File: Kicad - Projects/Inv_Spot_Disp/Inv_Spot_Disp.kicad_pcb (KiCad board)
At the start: 2 copper layers, 137.8 x 68.7 mm, 42 parts, among them J1 PWM_Out, J2 Power_Supply, J3 Current_Sense, J4 Prog, SW1 1, SW2 2, SW3 3, SW4 4, SW5 SW_Push, U1 STM32F030F4Px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

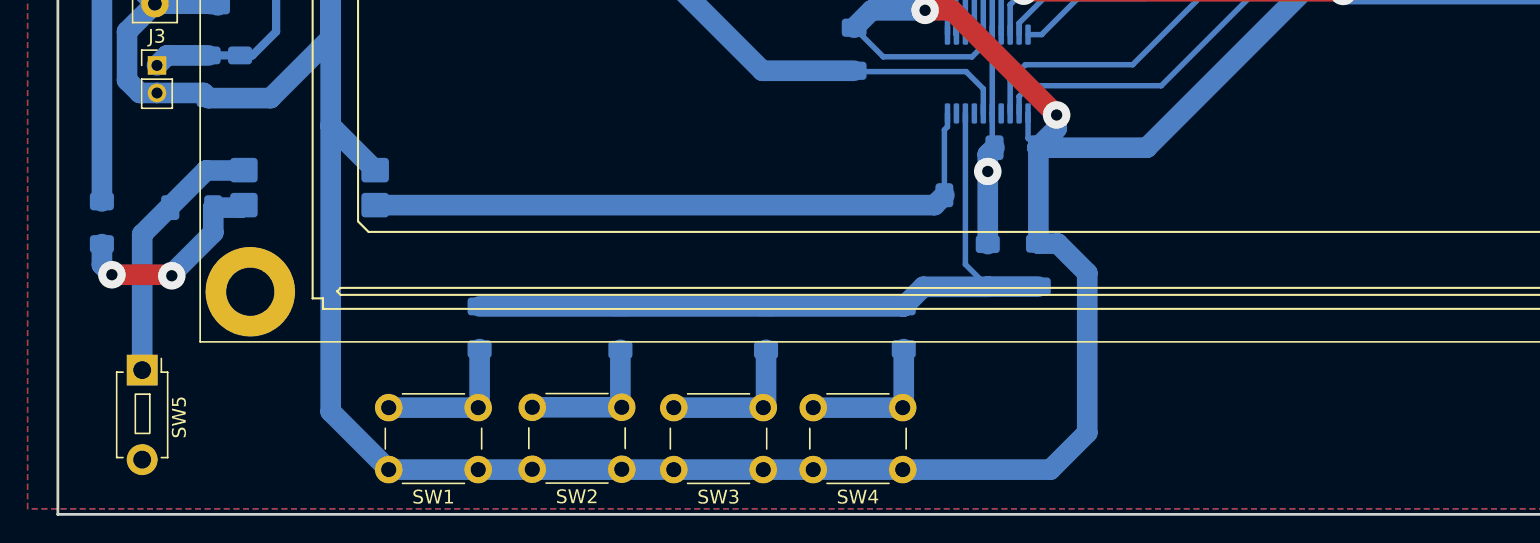
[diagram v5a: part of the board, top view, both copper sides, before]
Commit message: Ajustes de Isolamento e Espaçamento
Ajustes no isolamento de trilhas de alta tensão na placa de potência e no espaçamento dos capacitores dos IGBTs

Ajustes nas posições de componentes na placa de display

Ajustado ADC para aumentar período de amostragem
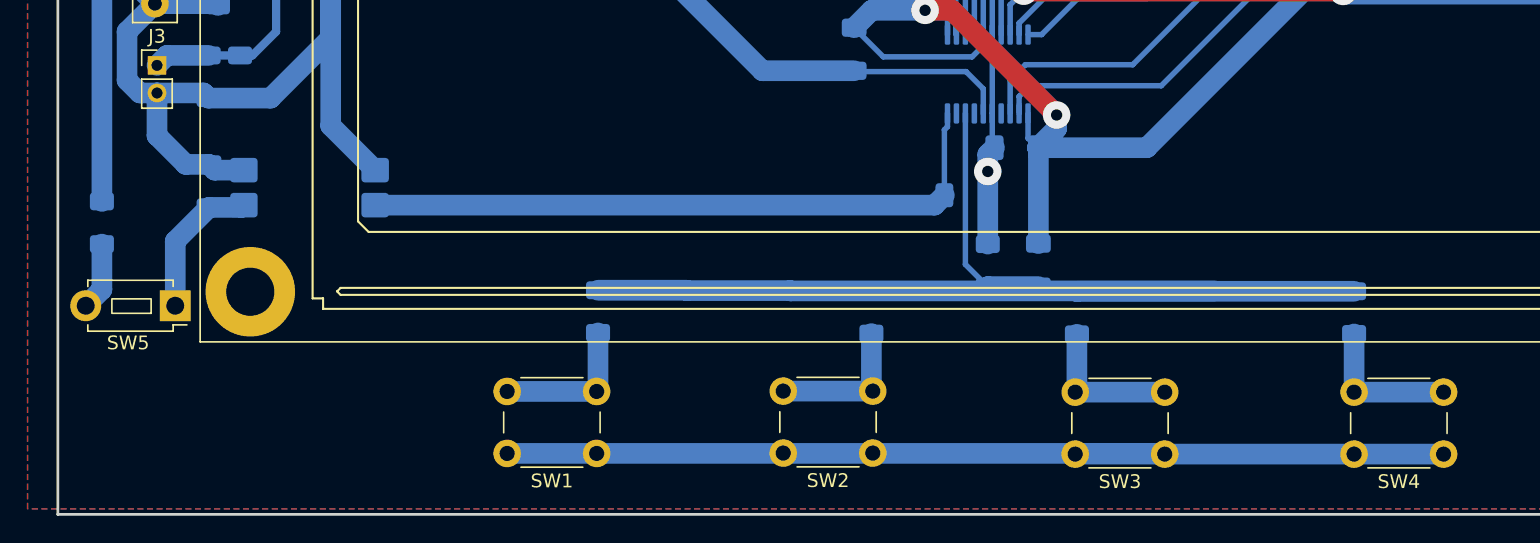
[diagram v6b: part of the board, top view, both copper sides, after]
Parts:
- moved SW4 39.3 mm to (129.1, 113.7)
- moved R5 32.7 mm to (122.6, 103.4)
- moved SW3 29.2 mm to (108.9, 113.7)
- moved R4 22.6 mm to (102.5, 103.4)
- moved R3 18.3 mm to (87.6, 103.4)
- moved SW2 18.3 mm to (87.7, 113.6)
- moved SW1 8.68 mm to (67.6, 113.6)
- moved R2 8.68 mm to (67.7, 103.3)
- moved SW5 5.26 mm to (37.0, 102.9), turned to 180 degrees
- moved C9 2.01 mm to (39.5, 94.2), turned to 90 degrees
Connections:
- C9 pad 2: Net-(C9-Pad2) -> GND
- R8 pad 1: Net-(C9-Pad1) -> Net-(R8-Pad1)
- SW5 pad 1: Net-(C9-Pad2) -> Net-(C9-Pad1)
- SW5 pad 2: Earth -> Net-(R8-Pad1)
- U6 pad 2: Net-(C9-Pad2) -> GND
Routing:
- net Display_ADC: track 54.4 -> 81.9 mm
- net Net-(C9-Pad2): track 19.2 -> 0.00 mm
- net GND: track 404.7 -> 394.4 mm
- net Net-(R8-Pad1): track 0.00 -> 4.96 mm
- net Net-(C9-Pad1): track 15.4 -> 10.8 mm, vias 2 -> 0

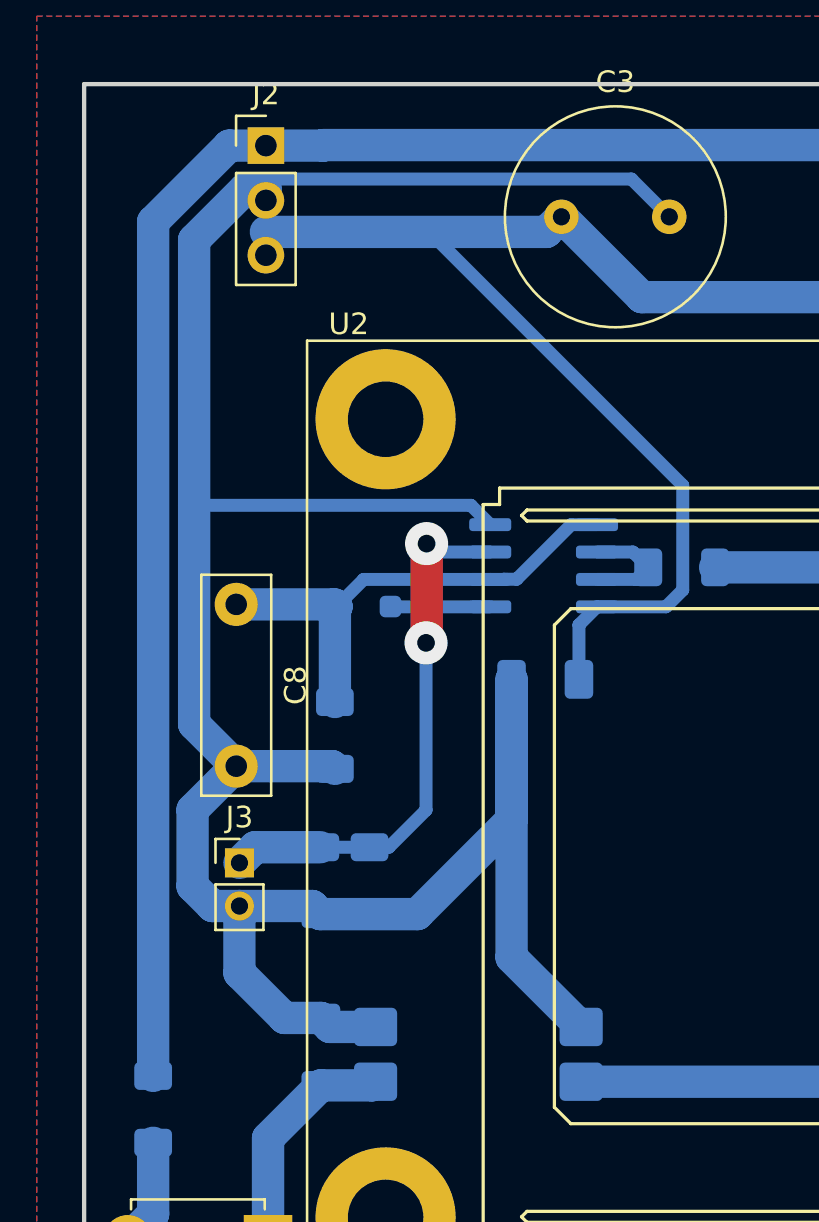
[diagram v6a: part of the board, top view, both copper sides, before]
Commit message: Ajustes de Esquemático / Layout
Ajustado símbolo da chave bimetálica na linha de 15V para proteção térmica

Ajustada trilhas de PWM que estavam sendo cobertas por um capacitor
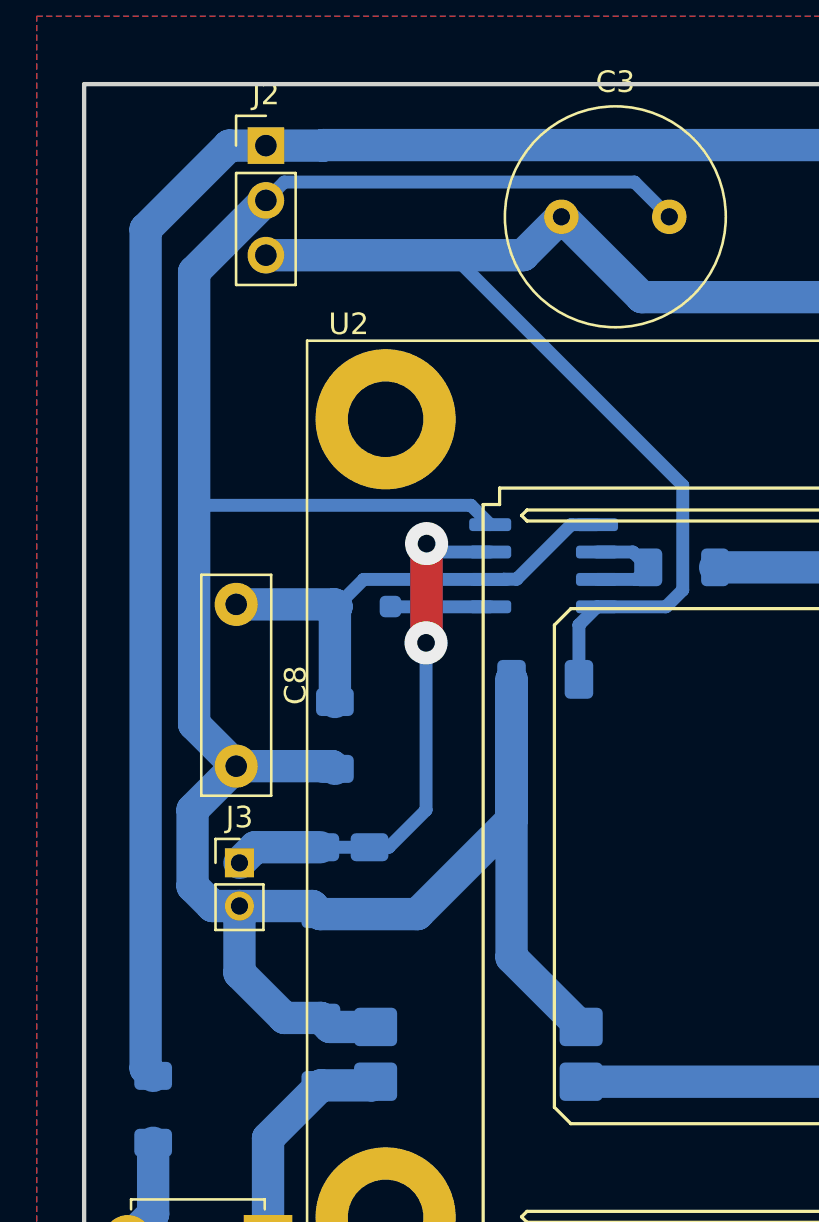
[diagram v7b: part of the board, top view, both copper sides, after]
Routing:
- net GND: track 394.4 -> 393.4 mm
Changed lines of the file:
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@@
-	)
-	(segment
-		(start 37.375 53.75)
-		(end 36.925 54.2)
-		(width 0.6)
-		(layer "B.Cu")
-		(net "GND")
 	)
 	(segment
@@
 	)
 	(segment
+		(start 33.6 58.05)
+		(end 33.6 68.875)
+		(width 1.5)
+		(layer "B.Cu")
+		(net "GND")
+	)
+	(segment
 		(start 97.575 55.2)
 		(end 97.575 62.775)
@@
 	)
 	(segment
+		(start 36.925 54.725)
+		(end 33.6 58.05)
+		(width 1.5)
+		(layer "B.Cu")
+		(net "GND")
+	)
+	(segment
 		(start 99.7 91.4875)
 		(end 99.6375 91.425)
@@
 	)
 	(segment
+		(start 55.625 55.5)
+		(end 54.015 53.89)
+		(width 0.6)
+		(layer "B.Cu")
+		(net "GND")
+	)
+	(segment
 		(start 97.8 74.425)
 		(end 97.8 64.05)
@@
 	)
 	(segment
-		(start 35.970406 54.2)
-		(end 33.6 56.570406)
-		(width 1.5)
-		(layer "B.Cu")
-		(net "GND")
-	)
-	(segment
 		(start 113.075 61.175)
 		(end 115.225 61.175)
@@
 	)
 	(segment
-		(start 55.625 55.5)
-		(end 53.875 53.75)
-		(width 0.6)
-		(layer "B.Cu")
-		(net "GND")
-	)
-	(segment
 		(start 111.6875 67.85)
 		(end 111.6875 64.0925)
@@
 	)
 	(segment
+		(start 54.015 53.89)
+		(end 37.775 53.89)
+		(width 0.6)
+		(layer "B.Cu")
+		(net "GND")
+	)
+	(segment
 		(start 40 80.9675)
 		(end 40.125 81.0925)
@@
 	)
 	(segment
+		(start 37.775 53.89)
+		(end 36.925 54.74)
+		(width 0.6)
+		(layer "B.Cu")
+		(net "GND")
+	)
+	(segment
 		(start 91.57 66.25)
 		(end 92.84 64.98)
@@
 	)
 	(segment
-		(start 33.6 56.570406)
-		(end 33.6 68.875)
-		(width 1.5)
-		(layer "B.Cu")
-		(net "GND")
-	)
-	(segment
 		(start 80.192677 58.205177)
 		(end 81.1375 59.15)
@@
 	)
 	(segment
-		(start 36.925 54.2)
-		(end 35.970406 54.2)
-		(width 1.5)
-		(layer "B.Cu")
-		(net "GND")
-	)
-	(segment
 		(start 87.5875 81.45)
 		(end 86.325 82.7125)
@@
 		(end 96.575 75.65)
 		(width 0.4)
-		(layer "B.Cu")
-		(net "GND")
-	)
-	(segment
-		(start 53.875 53.75)
-		(end 37.375 53.75)
-		(width 0.6)
 		(layer "B.Cu")
 		(net "GND")
@@
 	)
 	(segment
+		(start 48.845 57.28)
+		(end 36.925 57.28)
+		(width 1.5)
+		(layer "B.Cu")
+		(net "5V")
+	)
+	(segment
 		(start 63.725 59.225)
 		(end 54.35 59.225)
@@
 	)
 	(segment
-		(start 50.625 55.5)
-		(end 49.925 56.2)
-		(width 1.5)
+		(start 45.58 57.28)
+		(end 36.925 57.28)
+		(width 0.6)
 		(layer "B.Cu")
 		(net "5V")
@@
 	)
 	(segment
-		(start 44.5 56.2)
-		(end 36.925 56.2)
-		(width 0.6)
-		(layer "B.Cu")
-		(net "5V")
-	)
-	(segment
 		(start 120.385 58.64)
 		(end 119.515 59.51)
@@
 	(segment
 		(start 56.25 67.95)
-		(end 44.5 56.2)
-		(width 0.6)
+		(end 45.58 57.28)
+		(width 0.6)
+		(layer "B.Cu")
+		(net "5V")
+	)
+	(segment
+		(start 50.625 55.5)
+		(end 48.845 57.28)
+		(width 1.5)
 		(layer "B.Cu")
 		(net "5V")
@@
 		(start 114.435 63.885)
 		(end 114.435 67.4725)
-		(width 1.5)
-		(layer "B.Cu")
-		(net "5V")
-	)
-	(segment
-		(start 49.925 56.2)
-		(end 36.925 56.2)
 		(width 1.5)
 		(layer "B.Cu")
@@
 	)
 	(segment
-		(start 31.7 55.725)
-		(end 31.7 95.325)
-		(width 1.5)
-		(layer "B.Cu")
-		(net "15V")
-	)
-	(segment
 		(start 85.192677 58.219823)
 		(end 84.2625 59.15)
@@
 	)
 	(segment
+		(start 31.35 94.975)
+		(end 31.7 95.325)
+		(width 1.5)
+		(layer "B.Cu")
+		(net "15V")
+	)
+	(segment
+		(start 35.225 52.2)
+		(end 31.35 56.075)
+		(width 1.5)
+		(layer "B.Cu")
+		(net "15V")
+	)
+	(segment
 		(start 39.6 52.175)
 		(end 81.717677 52.175)
@@
 	)
 	(segment
+		(start 94.3 55.65)
+		(end 85.192677 55.65)
+		(width 0.6)
+		(layer "B.Cu")
+		(net "15V")
+	)
+	(segment
+		(start 95.38 67.85)
+		(end 95.38 62.5)
+		(width 0.6)
+		(layer "B.Cu")
+		(net "15V")
+	)
+	(segment
+		(start 36.925 52.2)
+		(end 39.575 52.2)
+		(width 1.5)
+		(layer "B.Cu")
+		(net "15V")
+	)
+	(segment
 		(start 36.925 52.2)
 		(end 35.225 52.2)
@@
 	)
 	(segment
-		(start 94.3 55.65)
-		(end 85.192677 55.65)
-		(width 0.6)
-		(layer "B.Cu")
-		(net "15V")
-	)
-	(segment
-		(start 95.38 67.85)
-		(end 95.38 62.5)
-		(width 0.6)
-		(layer "B.Cu")
-		(net "15V")
-	)
-	(segment
-		(start 36.925 52.2)
-		(end 39.575 52.2)
-		(width 1.5)
-		(layer "B.Cu")
-		(net "15V")
-	)
-	(segment
 		(start 81.717677 52.175)
 		(end 85.192677 55.65)
@@
 	)
 	(segment
-		(start 35.225 52.2)
-		(end 31.7 55.725)
+		(start 31.35 56.075)
+		(end 31.35 94.975)
 		(width 1.5)
 		(layer "B.Cu")
@@
 		(layer "B.Cu")
 		(net "15V")
+	)
+	(segment
+		(start 37.025 102.9)
+		(end 37.025 98.2125)
+		(width 1.5)
+		(layer "B.Cu")
+		(net "Net-(C9-Pad1)")
+	)
+	(segment
+		(start 39.475 95.7625)
+		(end 41.8425 95.7625)
+		(width 1.5)
+		(layer "B.Cu")
+		(net "Net-(C9-Pad1)")
+	)
+	(segment
+		(start 37.025 98.2125)
+		(end 39.475 95.7625)
+		(width 1.5)
+		(layer "B.Cu")
+		(net "Net-(C9-Pad1)")
+	)
+	(segment
+		(start 41.8425 95.7625)
+		(end 42.01 95.595)
+		(width 1.5)
+		(layer "B.Cu")
+		(net "Net-(C9-Pad1)")
+	)
+	(segment
+		(start 31.7 98.425)
+		(end 31.7 101.725)
+		(width 1.5)
+		(layer "B.Cu")
+		(net "Net-(R8-Pad1)")
+	)
+	(segment
+		(start 31.7 101.725)
+		(end 30.525 102.9)
+		(width 1.5)
+		(layer "B.Cu")
+		(net "Net-(R8-Pad1)")
 	)
 	(via
@@
 	)
 	(segment
-		(start 37.025 102.9)
-		(end 37.025 98.2125)
-		(width 1.5)
-		(layer "B.Cu")
-		(net "Net-(C9-Pad1)")
-	)
-	(segment
-		(start 39.475 95.7625)
-		(end 41.8425 95.7625)
-		(width 1.5)
-		(layer "B.Cu")
-		(net "Net-(C9-Pad1)")
-	)
-	(segment
-		(start 37.025 98.2125)
-		(end 39.475 95.7625)
-		(width 1.5)
-		(layer "B.Cu")
-		(net "Net-(C9-Pad1)")
-	)
-	(segment
-		(start 41.8425 95.7625)
-		(end 42.01 95.595)
-		(width 1.5)
-		(layer "B.Cu")
-		(net "Net-(C9-Pad1)")
-	)
-	(segment
 		(start 52.275 71.04)
 		(end 53.94 71.04)
@@
 		(net "Net-(D1-A)")
 	)
-	(segment
-		(start 31.7 98.425)
-		(end 31.7 101.725)
-		(width 1.5)
-		(layer "B.Cu")
-		(net "Net-(R8-Pad1)")
-	)
-	(segment
-		(start 31.7 101.725)
-		(end 30.525 102.9)
-		(width 1.5)
-		(layer "B.Cu")
-		(net "Net-(R8-Pad1)")
-	)
 	(zone

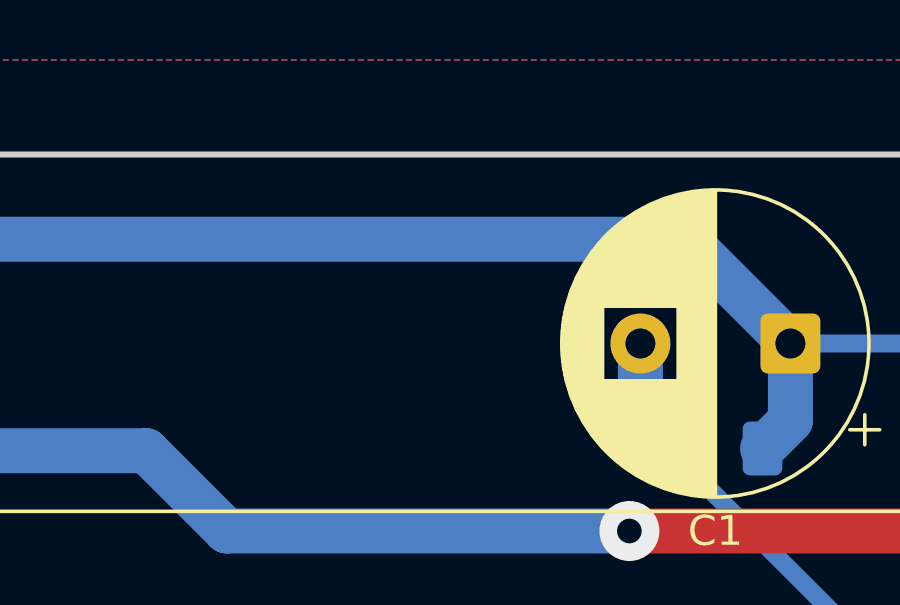
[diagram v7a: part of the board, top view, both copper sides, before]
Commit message: Adicionado LED - Temperatura
Adicionado LED na linha de 15V que desliga quando proteção térmica é acionada

Adicionados PDFs para impressão
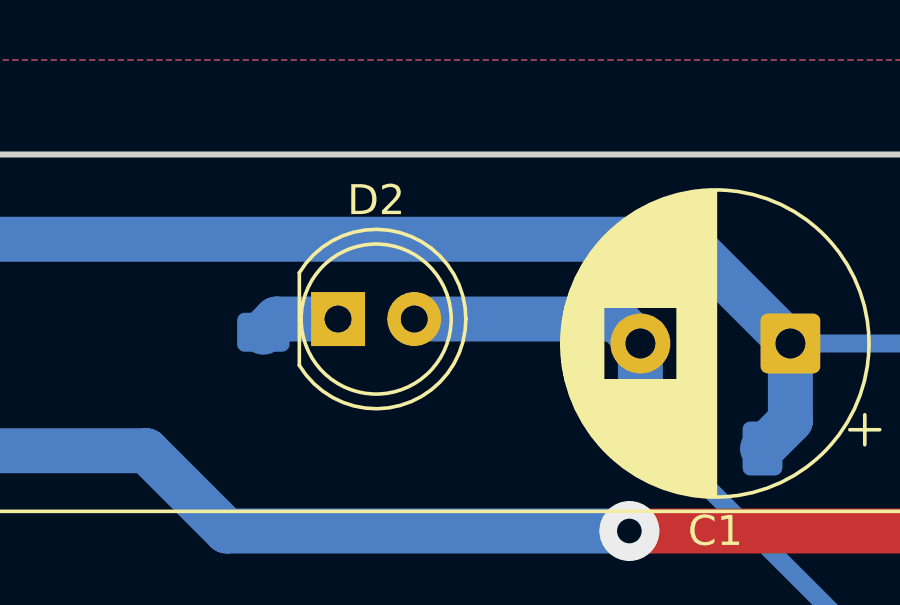
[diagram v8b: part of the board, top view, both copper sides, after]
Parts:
- added D2: LED, LED_THT:LED_D5.0mm, F.Cu at (70.1, 54.8)
- added R14: 1k5, Resistor_SMD:R_1206_3216Metric_Pad1.30x1.75mm_HandSolder, B.Cu at (67.6, 53.7)
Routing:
- net GND: track 393.4 -> 401.3 mm
- net Net-(D2-K): track 0.00 -> 2.67 mm
